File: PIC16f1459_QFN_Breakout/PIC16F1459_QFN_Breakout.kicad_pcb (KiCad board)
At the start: 2 copper layers, 33 x 20.3 mm, 9 parts, among them P1 CONN_01X05, P2 USB_OTG, P3 CONN_01X08, P4 CONN_01X08, U1 16F1459_QFN20

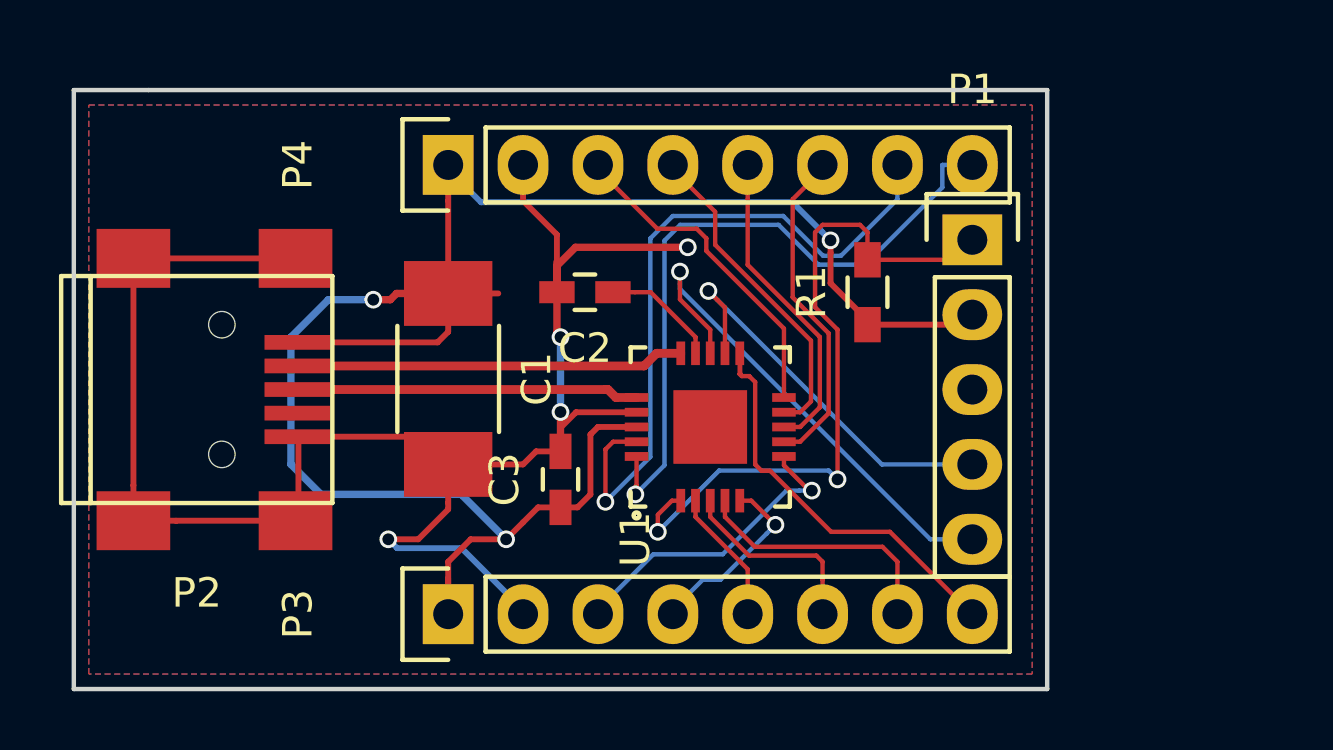
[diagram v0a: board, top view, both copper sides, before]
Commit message: Updated PIC16 breakout
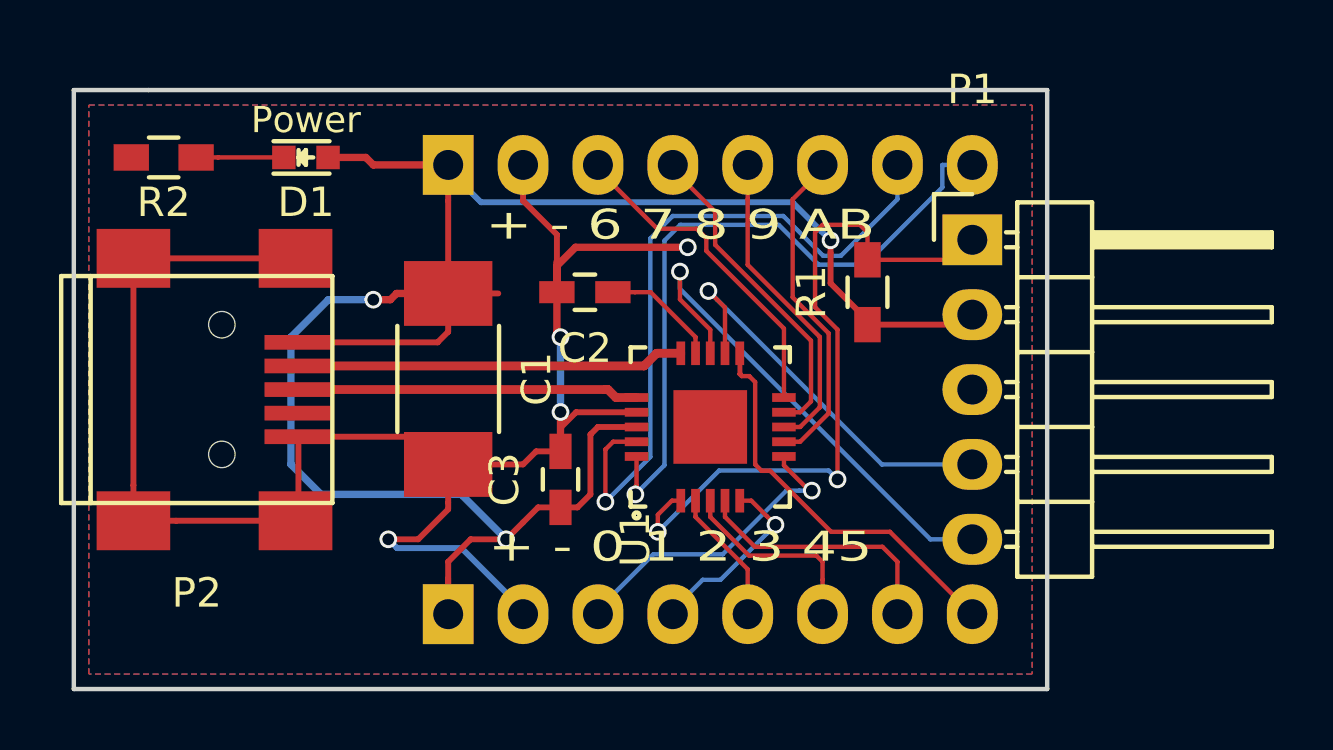
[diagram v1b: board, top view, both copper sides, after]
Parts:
- added D1: POWER, LEDs:LED-0603, F.Cu at (157.7, 101.3)
- added R2: 330R, Resistors_SMD:R_0603_HandSoldering, F.Cu at (152.9, 101.3)
- P1: footprint Pin_Headers:Pin_Header_Straight_1x05 -> Pin_Headers:Pin_Header_Angled_1x05
- P3, P4: moved to B.Cu
- turned P3 to 270 degrees
- turned P4 to 270 degrees
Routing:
- net +5V: track 64.9 -> 69.1 mm
- net Net-(D1-Pad1): track 0.00 -> 2.98 mm
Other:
- board text added: "+ - 0 1 2 3 45"
- board text added: "+ - 6 7 8 9 AB"
- board text added: "Power"

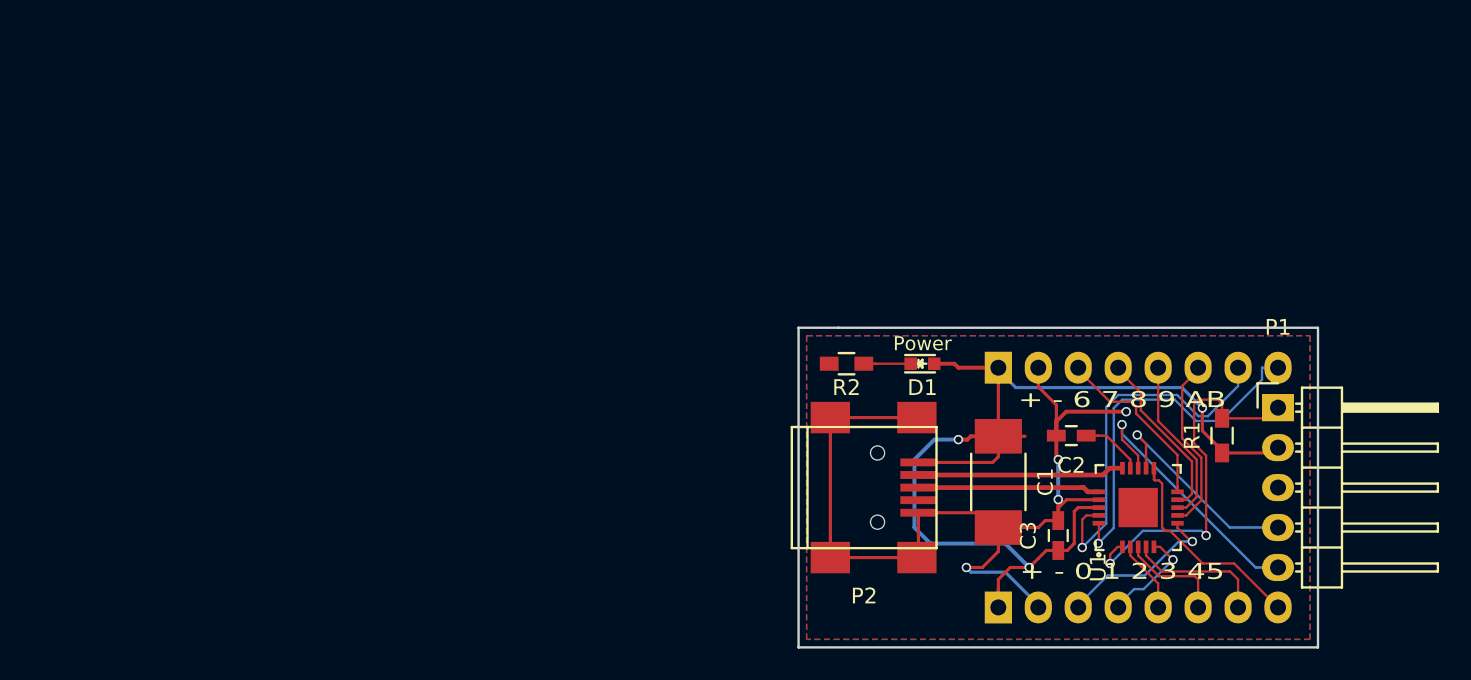
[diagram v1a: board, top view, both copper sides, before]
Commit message: Updated PIC16 breakout
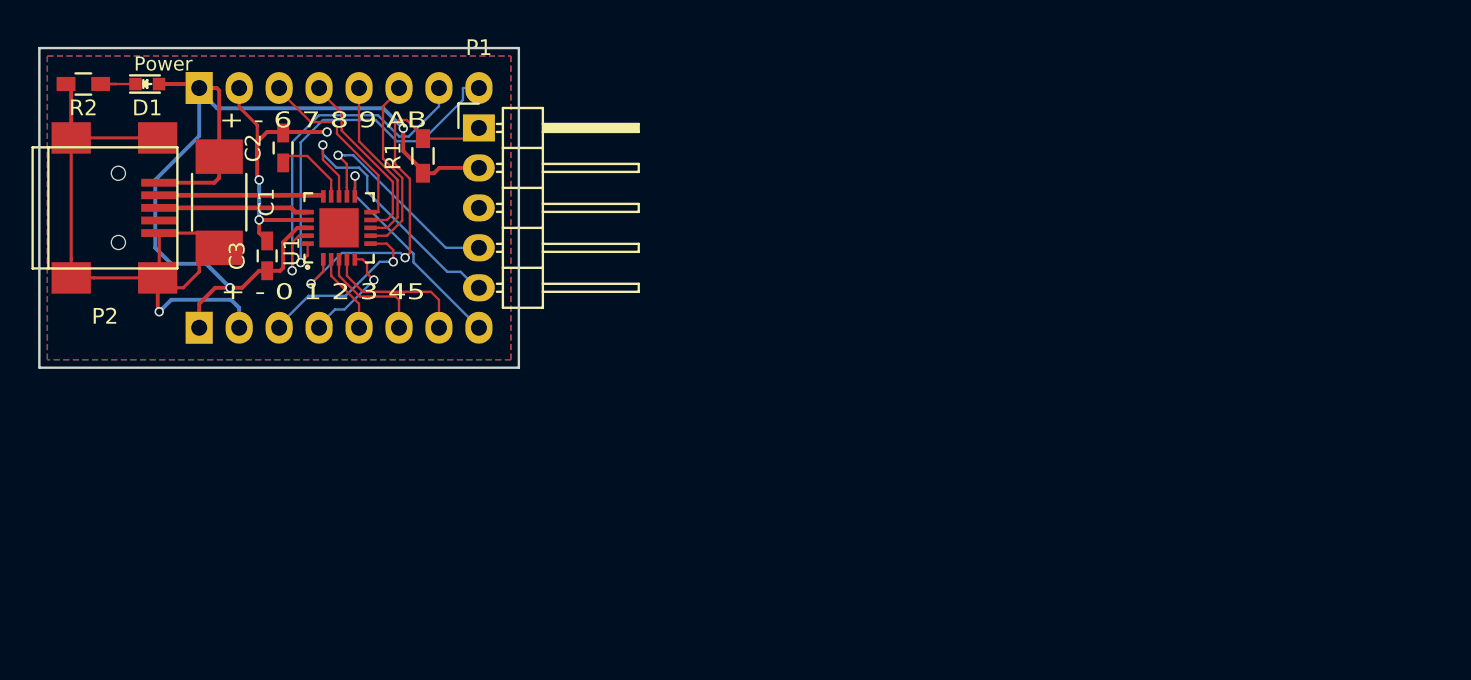
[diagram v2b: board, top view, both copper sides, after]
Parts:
- moved P1 53.8 mm to (129.5, 86.4)
- moved P3 53.8 mm to (111.8, 99.1)
- moved P4 53.8 mm to (111.8, 83.8)
- moved R1 53.8 mm to (126.0, 88.1)
- moved U1 53.8 mm to (120.7, 92.7)
- moved C3 53.3 mm to (116.1, 94.5)
- moved C2 53.3 mm to (117.1, 87.6), turned to 90 degrees
- moved C1 52.6 mm to (113.0, 91.1)
- moved D1 52.4 mm to (108.5, 83.6)
- moved R2 51.7 mm to (104.4, 83.6)
- moved P2 51.4 mm to (105.8, 91.4)
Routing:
- net GND: track 61.4 -> 65.4 mm
- net /D-: track 13.1 -> 10.5 mm
- net /D+: track 11.6 -> 9.54 mm
- net +5V: track 69.1 -> 67.4 mm, vias 3 -> 2
- net PGD: track 17.2 -> 18.3 mm
- net Net-(P3-Pad3): track 10.7 -> 11.4 mm
- net Net-(P3-Pad8): track 14.1 -> 14.8 mm, vias 0 -> 1
- net Net-(P3-Pad6): track 6.77 -> 7.31 mm
- net Net-(P4-Pad5): track 10.7 -> 11.3 mm
- net Net-(C2-Pad1): track 3.98 -> 4.48 mm
- net Net-(P4-Pad6): track 11.3 -> 11.8 mm
- net Net-(P4-Pad4): track 11.0 -> 11.5 mm
- net Net-(P4-Pad3): track 11.3 -> 11.8 mm
- net PGC: track 13.7 -> 14.2 mm
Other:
- board size 33 x 20.3 mm -> 30.5 x 20.3 mm

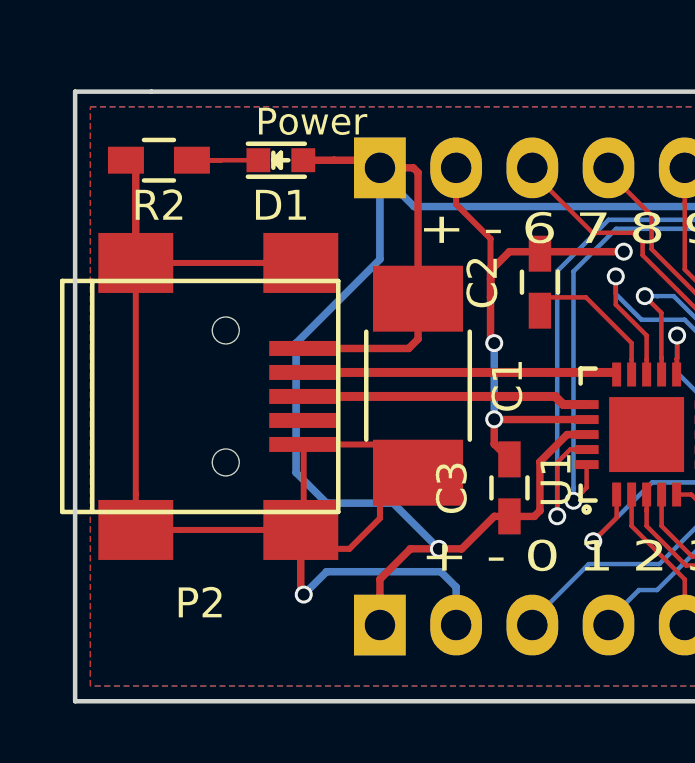
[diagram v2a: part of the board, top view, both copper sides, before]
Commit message: Update PIC16F USB Board and PIC 24F/32 USB board
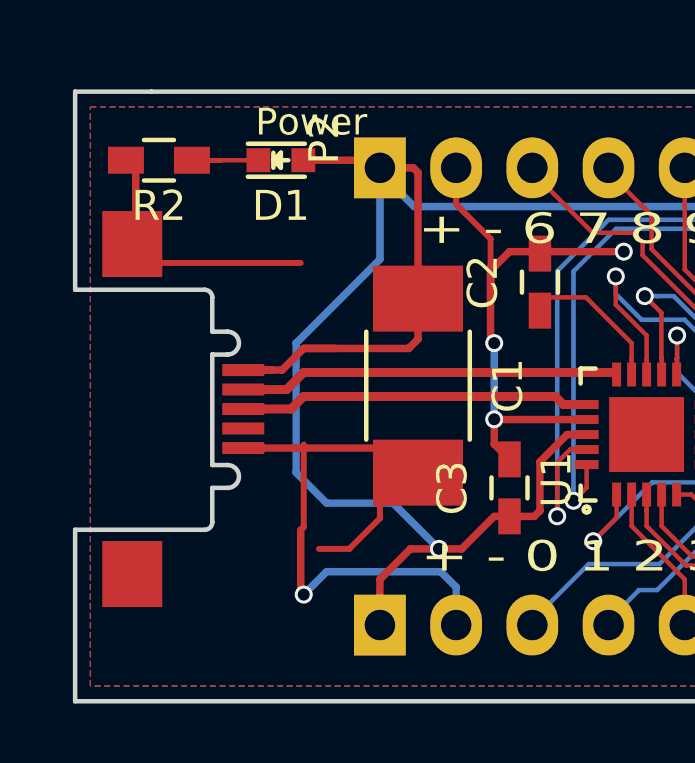
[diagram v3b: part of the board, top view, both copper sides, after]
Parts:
- added G***: LOGO, PIC24 USB:fingerchip_Logo, B.Cu at (114.3, 91.4)
- P2: footprint Connect:USB_Mini-B -> PIC16f1459_QFN_Breakout:USB_Micro_B_PCB_Recessed
- moved P2 1.91 mm to (103.9, 91.9), turned to 270 degrees
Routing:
- net GND: track 65.4 -> 53.0 mm
- net +5V: track 67.4 -> 70.7 mm
- net /D-: track 10.5 -> 12.7 mm
- net /D+: track 9.54 -> 11.7 mm
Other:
- outline, holes or cut-outs redrawn
